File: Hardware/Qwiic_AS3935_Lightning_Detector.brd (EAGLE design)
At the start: 25.4 x 25.4 mm, 67 parts, among them U1 AS3935

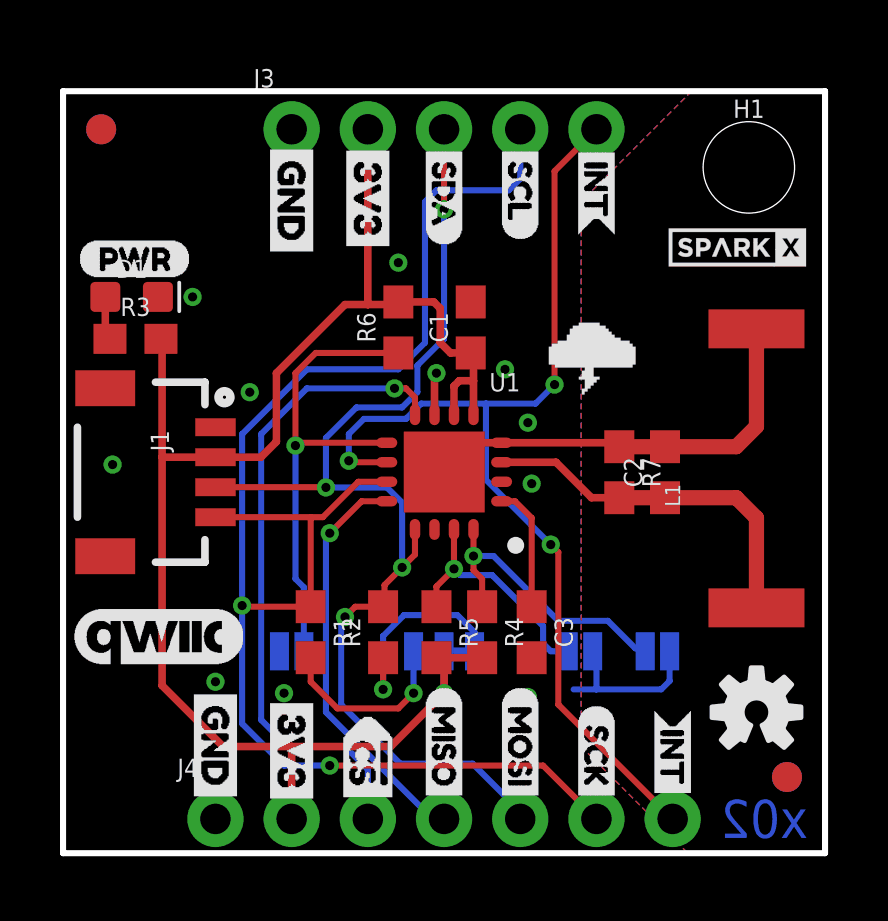
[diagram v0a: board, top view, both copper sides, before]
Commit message: Adds SparkFun related silk, adds parts that were added to Eagle libraries
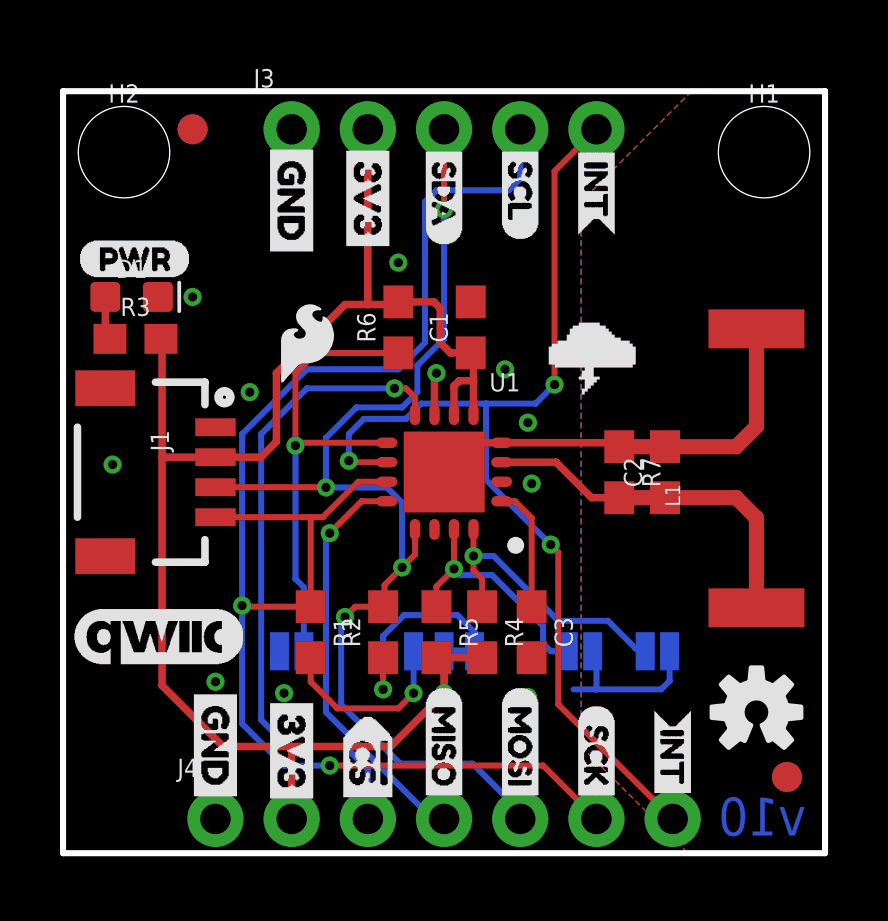
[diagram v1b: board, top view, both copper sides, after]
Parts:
- removed U$1: SPARKX-LOGO2, SparkX:SPARKX-TINY
- removed U$2: (no value), SparkX:SPARKX-TINY
- removed U$5: (no value), STORM:##0
- added H2: STAND-OFFTIGHT, SparkFun-Hardware:STAND-OFF-TIGHT
- added LOGO2: SFE_LOGO_NAME.1_INCH, SparkFun-Aesthetics:SFE_LOGO_NAME_.1
- added LOGO3: SFE_LOGO_FLAME.1_INCH, SparkFun-Aesthetics:SFE_LOGO_FLAME_.1
- L1: device temp_parts:MA5532-AE -> SparkFun-Coils:MA5532-AE
- U1: device temp_parts:16LD_MLPQ -> SparkFun-IC-Special-Function:16LD_MLPQ
- moved U$6 3.31 mm to (18.7, 15.1)
- moved U$7 3.06 mm to (19.8, 13.2)
- moved FD1 3.05 mm to (4.32, 24.1)
- moved FD4 3.05 mm to (4.32, 24.1)
- moved U$39 2.81 mm to (19.3, 11.2)
- moved H1 0.72 mm to (23.4, 23.4)
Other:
- board text added: "v10"
- board text removed: "x02"
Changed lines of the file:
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@@
 <setting verticaltext="up"/>
 </settings>
-<grid distance="0.05" unitdist="inch" unit="inch" style="lines" multiple="1" display="yes" altdistance="0.005" altunitdist="inch" altunit="inch"/>
+<grid distance="0.01" unitdist="inch" unit="inch" style="lines" multiple="1" display="yes" altdistance="0.001" altunitdist="inch" altunit="inch"/>
 <layers>
 <layer number="1" name="Top" color="4" fill="1" visible="yes" active="yes"/>
@@
 <wire x1="0" y1="25.4" x2="0" y2="0" width="0.2032" layer="20"/>
 <text x="19.177" y="-19.177" size="1.778" layer="51" font="vector">Elias Santistevan</text>
-<text x="23.368" y="1.143" size="1.27" layer="16" font="vector" rot="MR0" align="center">x02</text>
+<text x="24.765" y="0.5842" size="1.27" layer="16" font="vector" ratio="15" rot="MR0">v10</text>
 </plain>
 <attributes>
@@
 </element>
 <element name="LOGO1" library="SparkFun-Aesthetics" package="OSHW-LOGO-S" value="OSHW-LOGOS" x="23.114" y="4.699" smashed="yes"/>
-<element name="U$1" library="SparkX" package="SPARKX-TINY" value="SPARKX-LOGO2" x="22.479" y="20.193" smashed="yes"/>
-<element name="U$2" library="SparkX" package="SPARKX-TINY" value="" x="3.556" y="21.717" smashed="yes" rot="MR0"/>
 <element name="U$3" library="Labels" package="QWIIC_COPYRIGHT_SMALL" value="" x="3.175" y="7.239" smashed="yes"/>
 <element name="U$4" library="Labels" package="QWIIC_COPYRIGHT_SMALL" value="" x="3.175" y="17.526" smashed="yes" rot="MR0"/>
@@
 <element name="U$37" library="zero" package="00" value="" x="20.574" y="4.953" smashed="yes" rot="MR0"/>
 <element name="U$38" library="Labels" package="GND-03" value="" x="7.62" y="23.876" smashed="yes" rot="MR270"/>
-<element name="U$6" library="AS3935_4" package="AS39350" value="" x="18.415" y="18.415" smashed="yes" rot="MR0"/>
-<element name="U$7" library="LIghtning_4" package="LIGHTNING0" value="" x="19.558" y="16.256" smashed="yes" rot="MR0"/>
-<element name="U$39" library="Detector_4" package="DETECTOR0" value="" x="19.05" y="13.97" smashed="yes" rot="MR0"/>
+<element name="U$6" library="AS3935_4" package="AS39350" value="" x="18.669" y="15.113" smashed="yes" rot="MR0"/>
+<element name="U$7" library="LIghtning_4" package="LIGHTNING0" value="" x="19.812" y="13.208" smashed="yes" rot="MR0"/>
+<element name="U$39" library="Detector_4" package="DETECTOR0" value="" x="19.304" y="11.176" smashed="yes" rot="MR0"/>
 <element name="U$40" library="STORM" package="##0" value="" x="13.589" y="16.637" smashed="yes"/>
-<element name="U$5" library="STORM" package="##0" value="" x="17.272" y="11.557" smashed="yes" rot="MR0"/>
-<element name="H1" library="SparkFun-Hardware" package="STAND-OFF-TIGHT" value="STAND-OFFTIGHT" x="22.86" y="22.86" smashed="yes">
-<attribute name="NAME" x="22.86" y="24.511" size="0.6096" layer="25" font="vector" ratio="20" align="bottom-center"/>
-<attribute name="VALUE" x="22.86" y="21.209" size="0.6096" layer="27" font="vector" ratio="20" align="top-center"/>
-</element>
-<element name="FD1" library="SparkFun-Aesthetics" package="FIDUCIAL-1X2" value="FIDUCIAL1X2" x="1.27" y="24.13" smashed="yes" rot="MR0"/>
+<element name="H1" library="SparkFun-Hardware" package="STAND-OFF-TIGHT" value="STAND-OFFTIGHT" x="23.368" y="23.368" smashed="yes">
+<attribute name="NAME" x="23.368" y="25.019" size="0.6096" layer="25" font="vector" ratio="20" align="bottom-center"/>
+<attribute name="VALUE" x="23.368" y="21.717" size="0.6096" layer="27" font="vector" ratio="20" align="top-center"/>
+</element>
+<element name="FD1" library="SparkFun-Aesthetics" package="FIDUCIAL-1X2" value="FIDUCIAL1X2" x="4.318" y="24.13" smashed="yes" rot="MR0"/>
 <element name="FD2" library="SparkFun-Aesthetics" package="FIDUCIAL-1X2" value="FIDUCIAL1X2" x="24.13" y="2.54" smashed="yes" rot="MR0"/>
 <element name="FD3" library="SparkFun-Aesthetics" package="FIDUCIAL-1X2" value="FIDUCIAL1X2" x="24.13" y="2.54" smashed="yes"/>
-<element name="FD4" library="SparkFun-Aesthetics" package="FIDUCIAL-1X2" value="FIDUCIAL1X2" x="1.27" y="24.13" smashed="yes"/>
+<element name="FD4" library="SparkFun-Aesthetics" package="FIDUCIAL-1X2" value="FIDUCIAL1X2" x="4.318" y="24.13" smashed="yes"/>
 <element name="U$8" library="Labels" package="GND-03" value="" x="7.62" y="23.876" smashed="yes" rot="R270"/>
-<element name="L1" library="temp_parts" package="MA5532-AE" value="100uH" x="23.114" y="12.827" smashed="yes" rot="R90">
+<element name="L1" library="SparkFun-Coils" package="MA5532-AE" value="100uH" x="23.114" y="12.827" smashed="yes" rot="R90">
 <attribute name="NAME" x="20.574" y="11.557" size="0.508" layer="25" rot="R90"/>
 <attribute name="PROD_ID" value="NDUC-11334" x="23.114" y="12.827" size="1.778" layer="27" font="vector" ratio="15" rot="R90" display="off"/>
 <attribute name="VALUE" x="26.162" y="11.557" size="0.508" layer="27" rot="R90"/>
 </element>
-<element name="U1" library="temp_parts" package="16LD_MLPQ" value="AS3935" x="12.7" y="12.7" smashed="yes" rot="R180">
+<element name="U1" library="SparkFun-IC-Special-Function" package="16LD_MLPQ" value="AS3935" x="12.7" y="12.7" smashed="yes" rot="R180">
 <attribute name="NAME" x="15.24" y="16.002" size="0.6096" layer="25" font="vector" ratio="15" rot="R180"/>
 <attribute name="PROD_ID" value="IC-11333" x="12.7" y="12.7" size="1.778" layer="27" font="vector" ratio="15" rot="R180" display="off"/>
@@
 <element name="U$23" library="Labels" package="SCK-(]-03" value="" x="17.78" y="4.953" smashed="yes" rot="MR270"/>
 <element name="U$30" library="CS_2" package="#CS0" value="" x="10.16" y="4.826" smashed="yes" rot="MR270"/>
+<element name="LOGO2" library="SparkFun-Aesthetics" package="SFE_LOGO_NAME_.1" value="SFE_LOGO_NAME.1_INCH" x="13.462" y="17.526" smashed="yes" rot="MR0"/>
+<element name="LOGO3" library="SparkFun-Aesthetics" package="SFE_LOGO_FLAME_.1" value="SFE_LOGO_FLAME.1_INCH" x="8.128" y="17.018" smashed="yes"/>
+<element name="H2" library="SparkFun-Hardware" package="STAND-OFF-TIGHT" value="STAND-OFFTIGHT" x="2.032" y="23.368" smashed="yes">
+<attribute name="NAME" x="2.032" y="25.019" size="0.6096" layer="25" font="vector" ratio="20" align="bottom-center"/>
+<attribute name="VALUE" x="2.032" y="21.717" size="0.6096" layer="27" font="vector" ratio="20" align="top-center"/>
+</element>
 </elements>
 <signals>

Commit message: Replaces lightning detector - lightning detector was moved to correct library and so needed to be replaced in design
* Changes pull up resistor on the select interface line with a 10k
* Changes the wording of the address info box in the schematic to open/close rather
  than high/low
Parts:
- R6: value 1k -> 10k
- U1: device SparkFun-IC-Special-Function:16LD_MLPQ -> SparkFun-Sensors:16LD_MLPQ
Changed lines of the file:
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@@
 <attribute name="VALUE" x="2.413" y="16.383" size="0.6096" layer="27" font="vector" ratio="20" align="top-center"/>
 </element>
-<element name="R6" library="SparkFun-Resistors" package="0603" value="1k" x="11.176" y="17.526" smashed="yes" rot="R90">
+<element name="R6" library="SparkFun-Resistors" package="0603" value="10k" x="11.176" y="17.526" smashed="yes" rot="R90">
 <attribute name="NAME" x="10.414" y="17.526" size="0.6096" layer="25" font="vector" ratio="20" rot="R90" align="bottom-center"/>
-<attribute name="PROD_ID" value="RES-07856" x="11.176" y="17.526" size="1.778" layer="27" rot="R90" display="off"/>
-<attribute name="VALUE" x="11.938" y="17.526" size="0.6096" layer="27" font="vector" ratio="20" rot="R90" align="top-center"/>
+<attribute name="PROD_ID" value="RES-00824" x="11.176" y="17.526" size="1.778" layer="27" rot="R90" display="off"/>
+<attribute name="VALUE" value="10k" x="11.938" y="17.526" size="0.6096" layer="27" font="vector" ratio="20" rot="R90" align="top-center"/>
 </element>
 <element name="JP3" library="SparkFun-Jumpers" package="SMT-JUMPER_2_NO_SILK" value="JUMPER-SMT_2_NO_SILK" x="7.62" y="6.731" smashed="yes" rot="MR0">
@@
 <attribute name="VALUE" x="26.162" y="11.557" size="0.508" layer="27" rot="R90"/>
 </element>
-<element name="U1" library="SparkFun-IC-Special-Function" package="16LD_MLPQ" value="AS3935" x="12.7" y="12.7" smashed="yes" rot="R180">
+<element name="U1" library="SparkFun-Sensors" package="16LD_MLPQ" value="AS3935" x="12.7" y="12.7" smashed="yes" rot="R180">
 <attribute name="NAME" x="15.24" y="16.002" size="0.6096" layer="25" font="vector" ratio="15" rot="R180"/>
 <attribute name="PROD_ID" value="IC-11333" x="12.7" y="12.7" size="1.778" layer="27" font="vector" ratio="15" rot="R180" display="off"/>

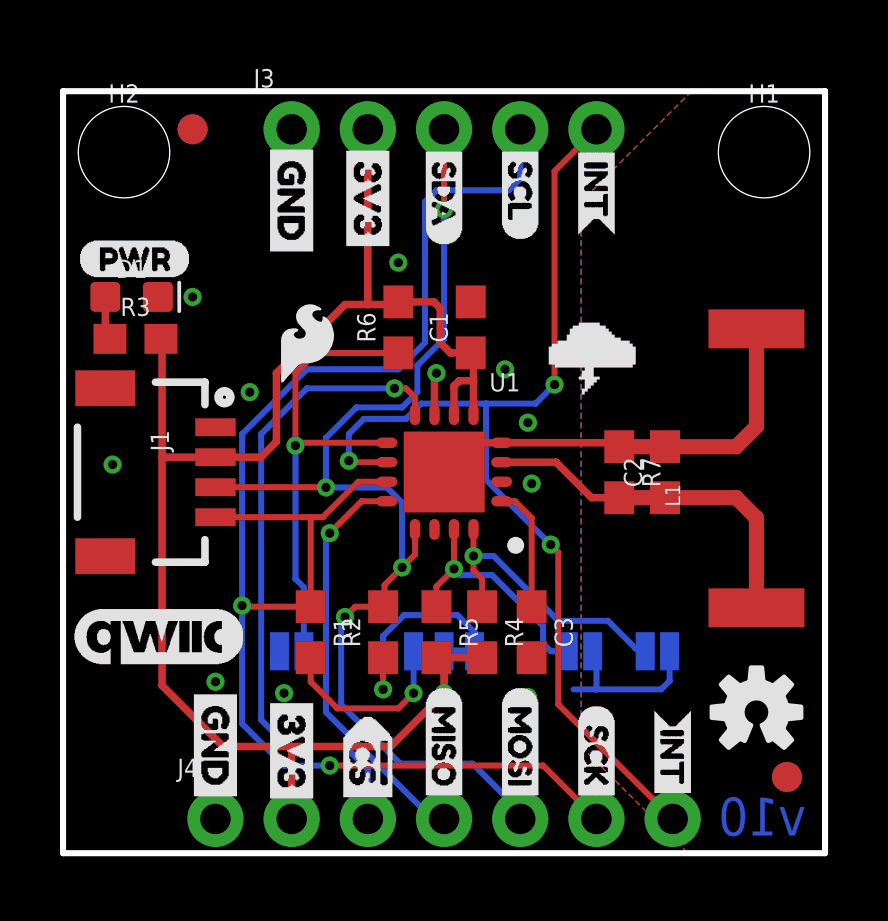
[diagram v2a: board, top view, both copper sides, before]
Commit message: Fixes clearance issues after changing DRC to SparkFun-tight.drc, Adds disconnect jumper to power LED
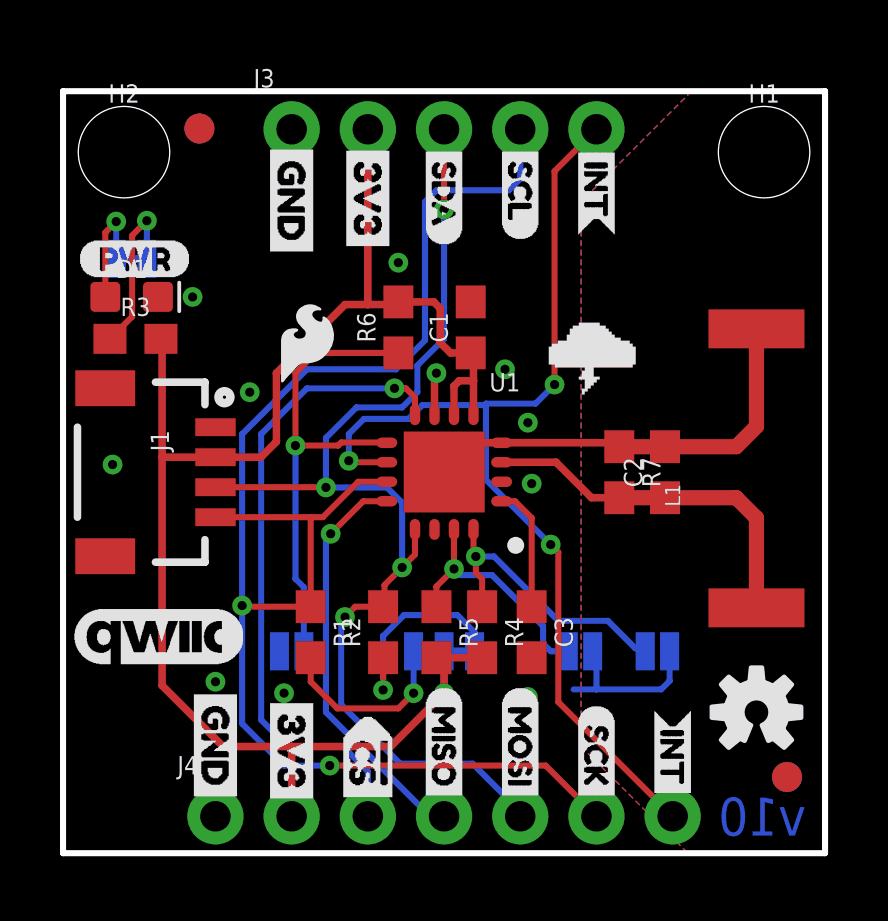
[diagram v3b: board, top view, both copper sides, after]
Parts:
- added JP5: LED, SparkFun-Jumpers:SMT-JUMPER_2_NC_TRACE_SILK
- added U$1: (no value), LED:LED0
- moved U$4 10.3 mm to (3.23, 7.22)
- moved FD4 0.23 mm to (4.55, 24.2)
- moved FD1 0.23 mm to (4.54, 24.2)
- moved J4 0.09 mm to (5.08, 1.23)
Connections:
- new net N$5: D1.A, JP5.1
- net N$1: now also JP5.2; no longer D1.A
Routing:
- net N$1: track 1.46 -> 5.72 mm, vias 0 -> 1
- net N$5: track 0.00 -> 3.91 mm, vias 0 -> 1
